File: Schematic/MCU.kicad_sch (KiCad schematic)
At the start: 21 parts, among them IC3 STM32H743VIT6, J1 USB_C_Receptacle_USB2.0_16P, SW1 TS24CA, Y1 8MHz

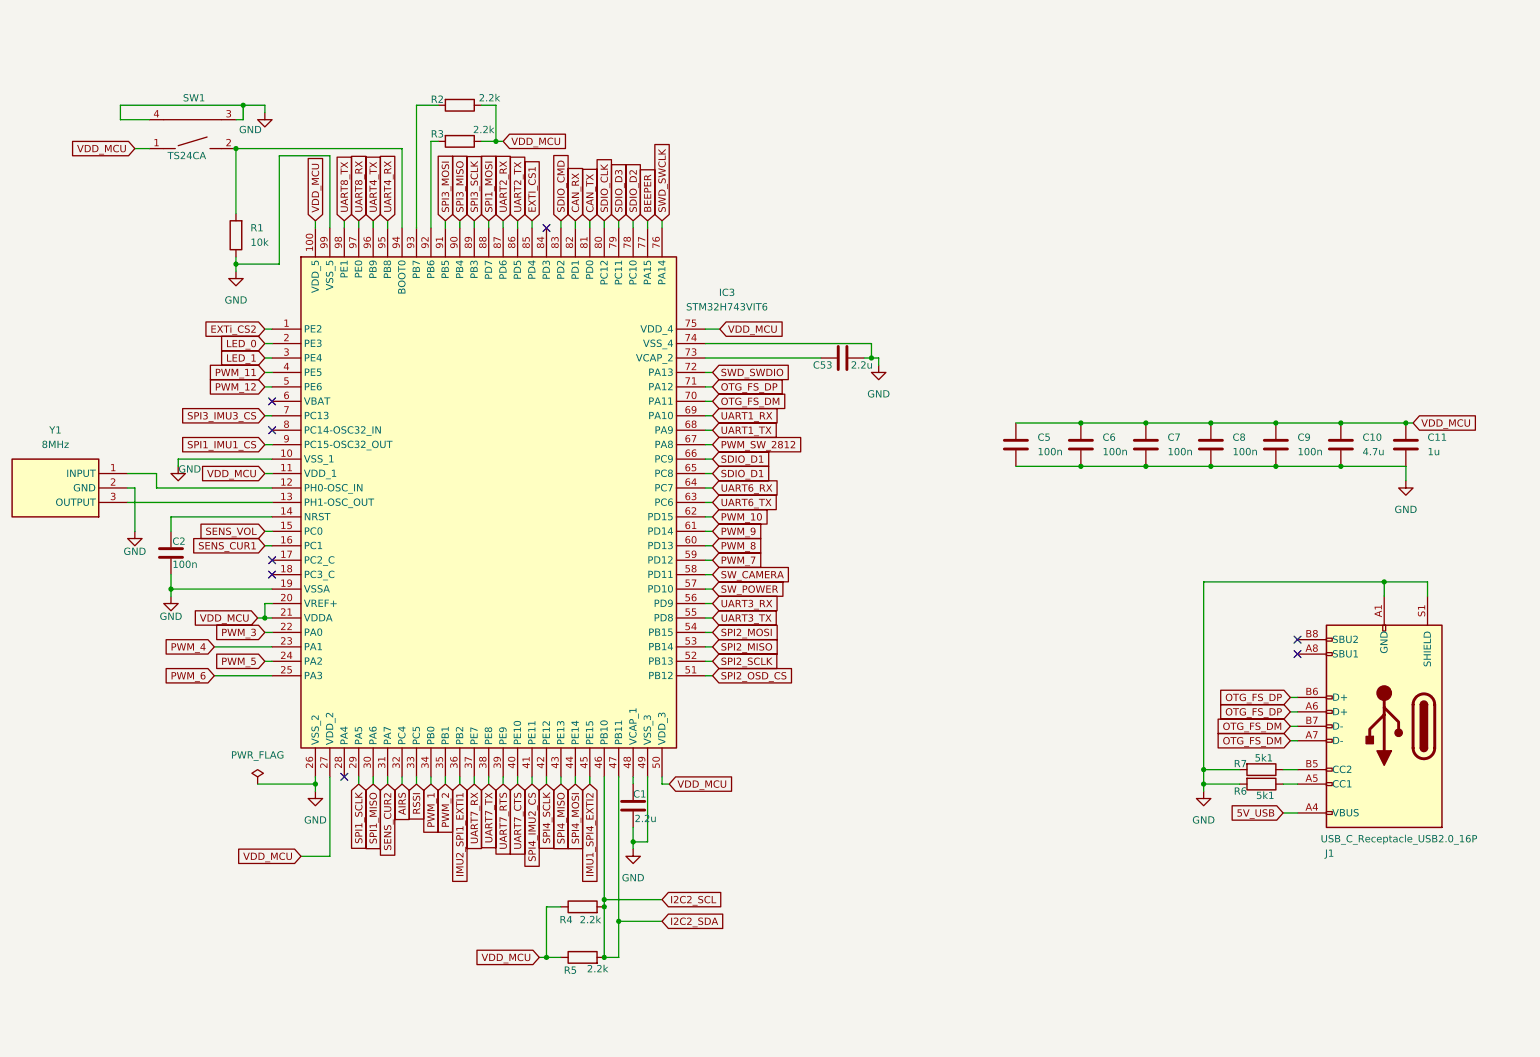
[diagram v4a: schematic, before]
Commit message: Refactor schematic files and update component placements
- Adjusted component positions in osd.kicad_sch for better layout.
- Added new junctions and wires in rf_rx.kicad_sch to improve connectivity.
- Introduced additional junctions and wires in sensors.kicad_sch for enhanced signal routing.
- Removed outdated backup file fch7-2025-11-18_191836.zip and added new backup fch7-2025-11-27_202230.zip.
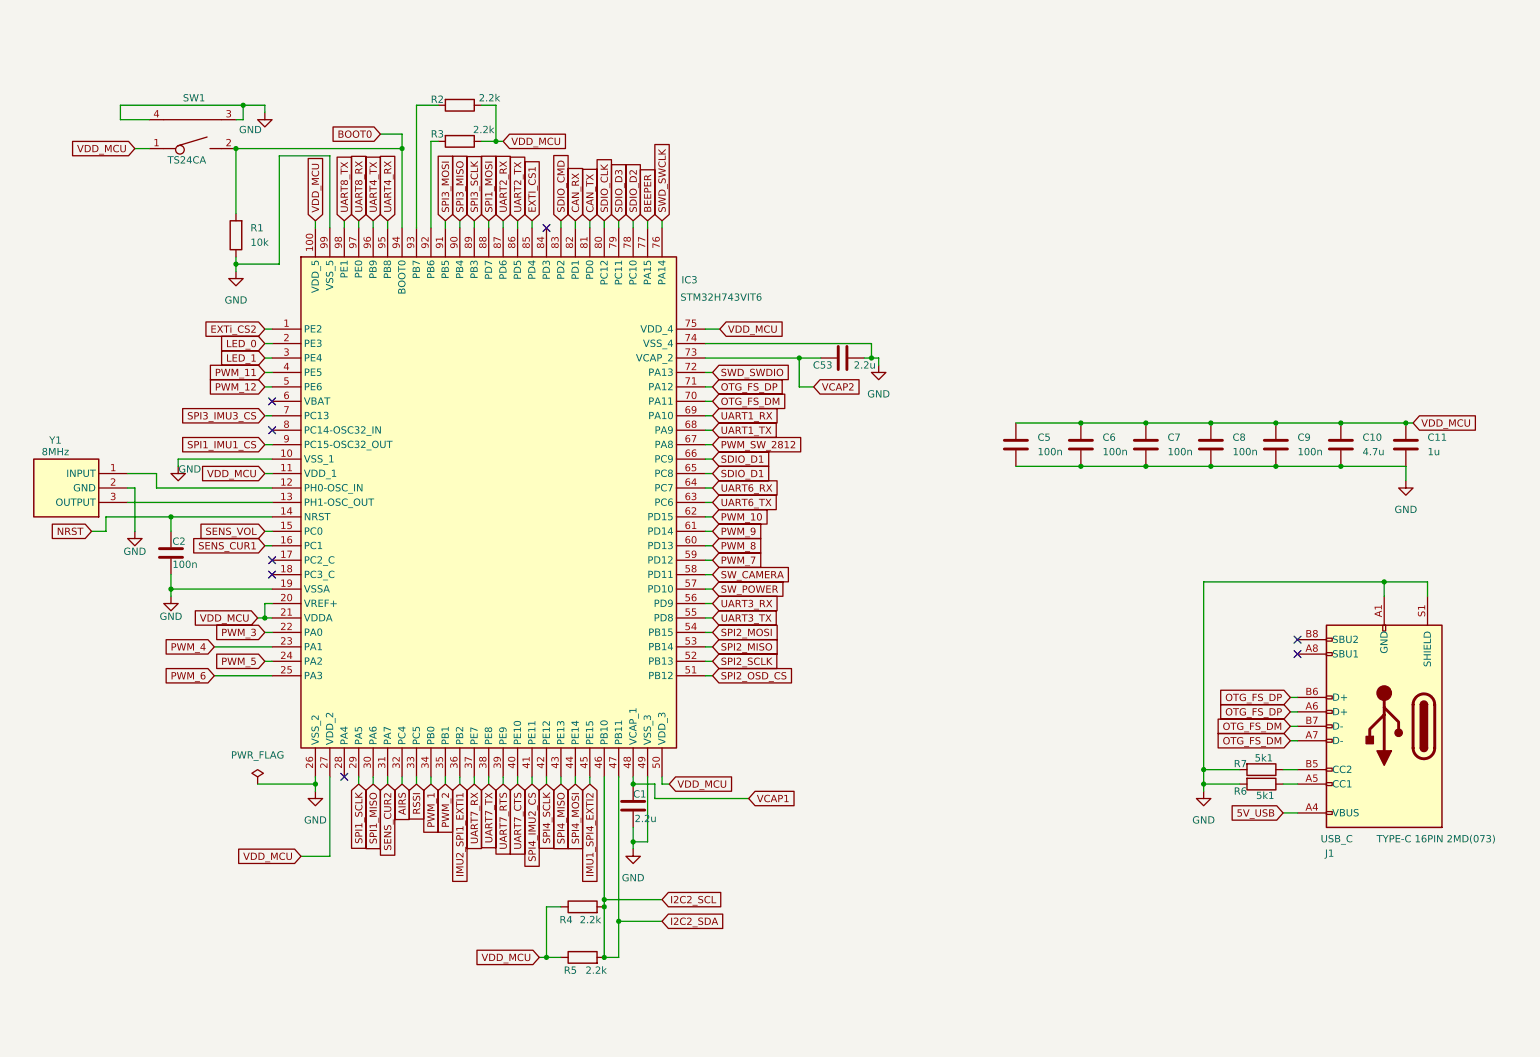
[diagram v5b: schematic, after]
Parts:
- J1: value USB_C_Receptacle_USB2.0_16P -> USB_C
- SW1: footprint fch7_fp:SW-SMD_2P-TS24CA -> ProLib_pcs_2025-11-24:SW-SMD_2P-TS24CA
- Y1: footprint fch7_fp:CSTNE8M00G55Z000R0 -> CSTNE8M00G55Z000R0
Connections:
- net NRST: now reaches C2.1, IC3.14 (NRST)
- net BOOT0: now reaches IC3.94 (BOOT0), R1.2, SW1.2
- net VCAP2: now reaches C53.1, IC3.73 (VCAP_2)
- net VCAP1: now reaches C1.1, IC3.48 (VCAP_1)
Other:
- moved on the sheet: Y1
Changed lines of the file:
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@@
 	)
 	(junction
+		(at 127 148.59)
+		(diameter 0)
+		(color 0 0 0 0)
+	)
+	(junction
 		(at 205.74 85.09)
 		(diameter 0)
@@
 	)
 	(junction
+		(at 156.21 73.66)
+		(diameter 0)
+		(color 0 0 0 0)
+	)
+	(junction
 		(at 259.08 113.03)
 		(diameter 0)
@@
 	)
 	(junction
+		(at 86.36 36.83)
+		(diameter 0)
+		(color 0 0 0 0)
+	)
+	(junction
 		(at 217.17 85.09)
 		(diameter 0)
@@
 	)
 	(junction
+		(at 45.72 101.6)
+		(diameter 0)
+		(color 0 0 0 0)
+	)
+	(junction
 		(at 111.76 179.07)
 		(diameter 0)
@@
 	(wire
 		(pts
+			(xy 156.21 78.74) (xy 156.21 73.66)
+		)
+		(stroke
+			(width 0)
+			(type default)
+		)
+	)
+	(wire
+		(pts
+			(xy 158.75 78.74) (xy 156.21 78.74)
+		)
+		(stroke
+			(width 0)
+			(type default)
+		)
+	)
+	(wire
+		(pts
 			(xy 60.96 119.38) (xy 62.23 119.38)
 		)
@@
 	(wire
 		(pts
+			(xy 147.32 151.13) (xy 130.81 151.13)
+		)
+		(stroke
+			(width 0)
+			(type default)
+		)
+	)
+	(wire
+		(pts
 			(xy 64.77 38.1) (xy 64.77 57.15)
 		)
@@
 	(wire
 		(pts
-			(xy 139.7 73.66) (xy 160.02 73.66)
+			(xy 139.7 73.66) (xy 156.21 73.66)
 		)
 		(stroke
@@
 	(wire
 		(pts
+			(xy 34.29 101.6) (xy 45.72 101.6)
+		)
+		(stroke
+			(width 0)
+			(type default)
+		)
+	)
+	(wire
+		(pts
 			(xy 101.6 49.53) (xy 101.6 50.8)
 		)
@@
 	(wire
 		(pts
+			(xy 130.81 148.59) (xy 127 148.59)
+		)
+		(stroke
+			(width 0)
+			(type default)
+		)
+	)
+	(wire
+		(pts
 			(xy 110.49 179.07) (xy 111.76 179.07)
 		)
@@
 	(wire
 		(pts
+			(xy 86.36 34.29) (xy 86.36 36.83)
+		)
+		(stroke
+			(width 0)
+			(type default)
+		)
+	)
+	(wire
+		(pts
 			(xy 73.66 38.1) (xy 64.77 38.1)
 		)
@@
 	(wire
 		(pts
+			(xy 130.81 151.13) (xy 130.81 148.59)
+		)
+		(stroke
+			(width 0)
+			(type default)
+		)
+	)
+	(wire
+		(pts
 			(xy 62.23 88.9) (xy 63.5 88.9)
 		)
@@
 	(wire
 		(pts
+			(xy 82.55 34.29) (xy 86.36 34.29)
+		)
+		(stroke
+			(width 0)
+			(type default)
+		)
+	)
+	(wire
+		(pts
 			(xy 127 158.75) (xy 129.54 158.75)
 		)
@@
 	(wire
 		(pts
+			(xy 156.21 73.66) (xy 160.02 73.66)
+		)
+		(stroke
+			(width 0)
+			(type default)
+		)
+	)
+	(wire
+		(pts
 			(xy 73.66 147.32) (xy 73.66 161.29)
 		)
@@
 	(wire
 		(pts
+			(xy 31.75 104.14) (xy 34.29 104.14)
+		)
+		(stroke
+			(width 0)
+			(type default)
+		)
+	)
+	(wire
+		(pts
 			(xy 104.14 49.53) (xy 104.14 50.8)
 		)
@@
 	(wire
 		(pts
+			(xy 34.29 104.14) (xy 34.29 101.6)
+		)
+		(stroke
+			(width 0)
+			(type default)
+		)
+	)
+	(wire
+		(pts
 			(xy 62.23 93.98) (xy 63.5 93.98)
 		)
@@
 		)
 	)
+	(global_label "NRST"
+		(shape input)
+		(at 31.75 104.14 180)
+		(fields_autoplaced yes)
+		(effects
+			(font
+				(size 1.27 1.27)
+			)
+			(justify right)
+		)
+		(property "Intersheetrefs" "${INTERSHEET_REFS}"
+			(at 23.9872 104.14 0)
+			(effects
+				(font
+					(size 1.27 1.27)
+				)
+				(justify right)
+				(hide yes)
+			)
+		)
+	)
 	(global_label "OTG_FS_DP"
 		(shape input)
@@
 		)
 	)
+	(global_label "VCAP2"
+		(shape input)
+		(at 158.75 78.74 0)
+		(fields_autoplaced yes)
+		(effects
+			(font
+				(size 1.27 1.27)
+			)
+			(justify left)
+		)
+		(property "Intersheetrefs" "${INTERSHEET_REFS}"
+			(at 167.6619 78.74 0)
+			(effects
+				(font
+					(size 1.27 1.27)
+				)
+				(justify left)
+				(hide yes)
+			)
+		)
+	)
 	(global_label "SPI2_SCLK"
 		(shape input)
@@
 		)
 	)
+	(global_label "VCAP1"
+		(shape input)
+		(at 147.32 151.13 0)
+		(fields_autoplaced yes)
+		(effects
+			(font
+				(size 1.27 1.27)
+			)
+			(justify left)
+		)
+		(property "Intersheetrefs" "${INTERSHEET_REFS}"
+			(at 156.2319 151.13 0)
+			(effects
+				(font
+					(size 1.27 1.27)
+				)
+				(justify left)
+				(hide yes)
+			)
+		)
+	)
 	(global_label "SPI1_MOSI"
 		(shape input)
@@
 		)
 	)
+	(global_label "BOOT0"
+		(shape input)
+		(at 82.55 34.29 180)
+		(fields_autoplaced yes)
+		(effects
+			(font
+				(size 1.27 1.27)
+			)
+			(justify right)
+		)
+		(property "Intersheetrefs" "${INTERSHEET_REFS}"
+			(at 73.4567 34.29 0)
+			(effects
+				(font
+					(size 1.27 1.27)
+				)
+				(justify right)
+				(hide yes)
+			)
+		)
+	)
 	(global_label "SPI3_MOSI"
 		(shape input)
@@
 			)
 		)
-		(property "Value" "USB_C_Receptacle_USB2.0_16P"
+		(property "Value" "USB_C"
 			(at 247.904 158.242 0)
 			(effects
@@
 		)
 		(property "MPN" "TYPE-C 16PIN 2MD(073)"
-			(at 259.08 138.43 0)
+			(at 268.224 158.242 0)
 			(effects
 				(font
 					(size 1.27 1.27)
 				)
-				(hide yes)
 			)
 		)
@@
 		(on_board yes)
 		(dnp no)
-		(fields_autoplaced yes)
 		(property "Reference" "Y1"
-			(at 25.4 86.36 0)
+			(at 25.4 88.138 0)
 			(effects
 				(font
@@
 		)
 		(property "Value" "8MHz"
-			(at 25.4 88.9 0)
+			(at 25.4 90.17 0)
 			(effects
 				(font
@@
 			)
 		)
-		(property "Footprint" "fch7_fp:CSTNE8M00G55Z000R0"
+		(property "Footprint" "CSTNE8M00G55Z000R0"
 			(at 16.51 4.14 0)
 			(effects
@@
 		)
 		(property "Value" "2.2u"
-			(at 169.164 74.93 90)
+			(at 169.672 74.93 90)
 			(effects
 				(font
@@
 		)
 		(property "Value" "2.2k"
-			(at 118.872 181.102 90)
+			(at 118.618 181.356 90)
 			(effects
 				(font
@@
 		)
 		(property "Value" "TS24CA"
-			(at 48.514 38.1 0)
+			(at 48.514 38.862 0)
 			(effects
 				(font
@@
 			)
 		)
-		(property "Footprint" "fch7_fp:SW-SMD_2P-TS24CA"
+		(property "Footprint" "ProLib_pcs_2025-11-24:SW-SMD_2P-TS24CA"
 			(at 48.768 27.686 0)
 			(effects
@@
 		(on_board yes)
 		(dnp no)
-		(fields_autoplaced yes)
 		(property "Reference" "IC3"
-			(at 143.51 62.1598 0)
+			(at 136.906 59.944 0)
 			(effects
 				(font
@@
 		)
 		(property "Value" "STM32H743VIT6"
-			(at 143.51 64.6998 0)
+			(at 142.494 62.992 0)
 			(effects
 				(font

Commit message: Refactor code structure for improved readability and maintainability
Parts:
- SW1: footprint ProLib_pcs_2025-11-24:SW-SMD_2P-TS24CA -> fch7_fp:SW-SMD_2P-TS24CA
- Y1: footprint CSTNE8M00G55Z000R0 -> fch7_fp:CSTNE8M00G55Z000R0
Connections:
- net I2C2_SCL: no longer IC3.47 (PB11), R5.2
- new net I2C2_SDA: IC3.47 (PB11), R5.2
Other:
- note added: "Decoupling capacitors for MCU pins"
- moved on the sheet: C10, C11, C5, C6, C7, C8, C9, R4

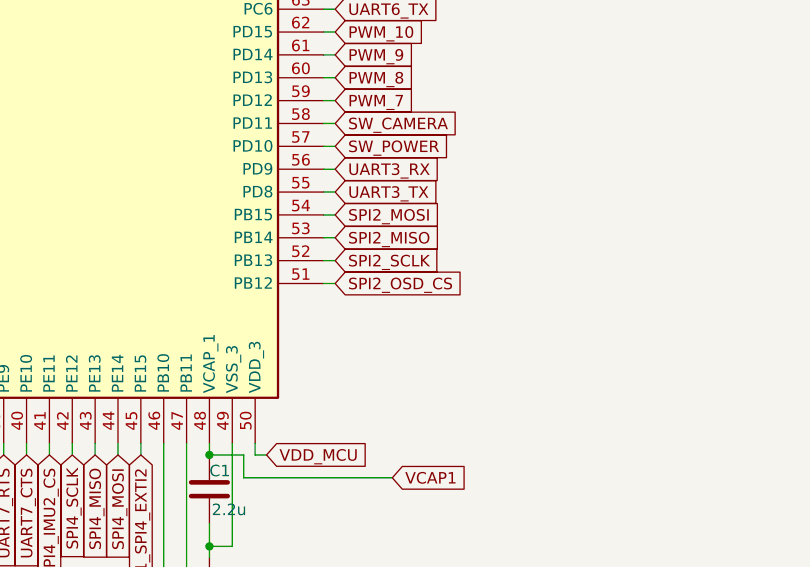
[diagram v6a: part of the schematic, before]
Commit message: Removed useless analog OSD and VTX conneections to support only digital DJI
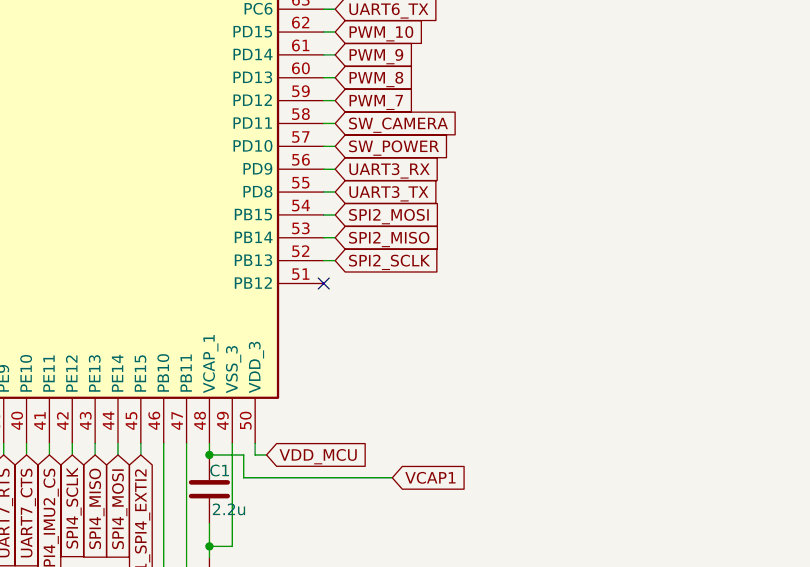
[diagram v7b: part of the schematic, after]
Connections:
- net SPI2_OSD_CS: no longer names the net of IC3.51 (PB12)
- no-connect marks 8 -> 9
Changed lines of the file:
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@@
 	)
 	(no_connect
+		(at 139.7 129.54)
+	)
+	(no_connect
 		(at 111.76 50.8)
 	)
@@
 	(wire
 		(pts
-			(xy 139.7 129.54) (xy 140.97 129.54)
-		)
-		(stroke
-			(width 0)
-			(type default)
-		)
-	)
-	(wire
-		(pts
 			(xy 227.33 146.05) (xy 227.33 148.59)
 		)
@@
 			(effects
 				(font
-					(size 1.27 1.27)
-				)
-				(justify left)
-				(hide yes)
-			)
-		)
-	)
-	(global_label "SPI2_OSD_CS"
-		(shape input)
-		(at 140.97 129.54 0)
-		(fields_autoplaced yes)
-		(effects
-			(font
-				(size 1.27 1.27)
-			)
-			(justify left)
-		)
-		(property "Intersheetrefs" "${INTERSHEET_REFS}"
-			(at 156.4737 129.54 0)
-			(effects
-				(font

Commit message: Refactor code structure for improved readability and maintainability
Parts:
- removed IC3: STM32H743VIT6, fch7_fp:LQFP-100_14x14mm_P0.5mm_STM32H743, symbol STM32H743VIT6:STM32H743VIT6
- removed J1: USB_C, fch7_fp:USB-C-SMD_TYPE-C-6PIN-2MD-073, symbol Connector:USB_C_Receptacle_USB2.0_16P
- removed SW1: TS24CA, fch7_fp:SW-SMD_2P-TS24CA, symbol fch7_sym:TS24CA
- removed Y1: 8MHz, fch7_fp:CSTNE8M00G55Z000R0, symbol CSTNE8M00G55Z000R0:CSTNE8M00G55Z000R0
- added IC3: STM32H743VIT6, fch7_fp:LQFP-100_14x14mm_P0.5mm_STM32H743, symbol fclib:STM32H743VIT6
- added SW1: TS24CA, fch7_fp:SW-SMD_2P-TS24CA, symbol fclib:TS24CA
- added USB1: USB-C-SMD_TYPE-C-6PIN-2MD-073, fch7_fp:USB-C-SMD_TYPE-C-6PIN-2MD-073, symbol fclib:TYPE-C 16PIN 2MD(073)
- added Y1: 8MHz, fch7_fp:CSTNE8M00G55Z000R0, symbol fclib:CSTNE8M00G55Z000R0
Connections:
- net 5V_USB: now also USB1.11 (VBUS), USB1.2 (VBUS)
- net AIRS: now also IC3.32 (PC4)
- net BEEPER: now also IC3.77 (PA15)
- net BOOT0: now also IC3.94 (BOOT0), SW1.2
- net CAN_RX: now also IC3.82 (PD1)
- net CAN_TX: now also IC3.81 (PD0)
- net EXTI_CS1: now also IC3.85 (PD4)
- net EXTi_CS2: now also IC3.1 (PE2)
- net GND: now also IC3.10 (VSS_1), IC3.19 (VSSA), IC3.26 (VSS_2), IC3.49 (VSS_3), IC3.74 (VSS_4), IC3.99 (VSS_5), SW1.3, SW1.4, USB1.1 (GND), USB1.12 (GND), USB1.13 (SHELL), USB1.14 (SHELL), Y1.2 (GND)
- net I2C2_SCL: now also IC3.46 (PB10)
- net I2C2_SDA: now also IC3.47 (PB11)
- net IMU1_SPI4_EXTI2: now also IC3.45 (PE15)
- net IMU2_SPI1_EXTI1: now also IC3.36 (PB2)
- net LED_0: now also IC3.2 (PE3)
- net LED_1: now also IC3.3 (PE4)
- net NRST: now also IC3.14 (NRST)
- net OTG_FS_DM: now also IC3.70 (PA11), USB1.5 (DN2), USB1.7 (DN1)
- net OTG_FS_DP: now also IC3.71 (PA12), USB1.6 (DP1), USB1.8 (DP2)
- net PWM_1: now also IC3.34 (PB0)
- net PWM_10: now also IC3.62 (PD15)
- net PWM_11: now also IC3.4 (PE5)
- net PWM_12: now also IC3.5 (PE6)
- net PWM_2: now also IC3.35 (PB1)
- net PWM_3: now also IC3.22 (PA0)
- net PWM_4: now also IC3.23 (PA1)
- net PWM_5: now also IC3.24 (PA2)
- net PWM_6: now also IC3.25 (PA3)
- net PWM_7: now also IC3.59 (PD12)
- net PWM_8: now also IC3.60 (PD13)
- net PWM_9: now also IC3.61 (PD14)
- net PWM_SW_2812: now also IC3.67 (PA8)
- net RSSI: now also IC3.33 (PC5)
- net SDIO_CLK: now also IC3.80 (PC12)
- net SDIO_CMD: now also IC3.83 (PD2)
- net SDIO_D1: now also IC3.65 (PC8), IC3.66 (PC9)
- net SDIO_D2: now also IC3.78 (PC10)
- net SDIO_D3: now also IC3.79 (PC11)
- net SENS_CUR1: now also IC3.16 (PC1)
- net SENS_CUR2: now also IC3.31 (PA7)
- net SENS_VOL: now also IC3.15 (PC0)
- net SPI1_IMU1_CS: now also IC3.9 (PC15-OSC32_OUT)
- net SPI1_MISO: now also IC3.30 (PA6)
- net SPI1_MOSI: now also IC3.88 (PD7)
- net SPI1_SCLK: now also IC3.29 (PA5)
- net SPI2_MISO: now also IC3.53 (PB14)
- net SPI2_MOSI: now also IC3.54 (PB15)
- net SPI2_SCLK: now also IC3.52 (PB13)
- net SPI3_IMU3_CS: now also IC3.7 (PC13)
- net SPI3_MISO: now also IC3.90 (PB4)
- net SPI3_MOSI: now also IC3.91 (PB5)
- net SPI3_SCLK: now also IC3.89 (PB3)
- net SPI4_IMU2_CS: now also IC3.41 (PE11)
- net SPI4_MISO: now also IC3.43 (PE13)
- net SPI4_MOSI: now also IC3.44 (PE14)
- net SPI4_SCLK: now also IC3.42 (PE12)
- net SWD_SWCLK: now also IC3.76 (PA14)
- net SWD_SWDIO: now also IC3.72 (PA13)
- net SW_CAMERA: now also IC3.58 (PD11)
- net SW_POWER: now also IC3.57 (PD10)
- net UART1_RX: now also IC3.69 (PA10)
- net UART1_TX: now also IC3.68 (PA9)
- net UART2_RX: now also IC3.87 (PD6)
- net UART2_TX: now also IC3.86 (PD5)
- net UART3_RX: now also IC3.56 (PD9)
- net UART3_TX: now also IC3.55 (PD8)
- net UART4_RX: now also IC3.95 (PB8)
- net UART4_TX: now also IC3.96 (PB9)
- net UART6_RX: now also IC3.64 (PC7)
- net UART6_TX: now also IC3.63 (PC6)
- net UART7_CTS: now also IC3.40 (PE10)
- net UART7_RTS: now also IC3.39 (PE9)
- net UART7_RX: now also IC3.37 (PE7)
- net UART7_TX: now also IC3.38 (PE8)
- net UART8_RX: now also IC3.97 (PE0)
- net UART8_TX: now also IC3.98 (PE1)
- net VCAP1: now also IC3.48 (VCAP_1)
- net VCAP2: now also IC3.73 (VCAP_2)
- net VDD_MCU: now also IC3.100 (VDD_5), IC3.11 (VDD_1), IC3.20 (VREF+), IC3.21 (VDDA), IC3.27 (VDD_2), IC3.50 (VDD_3), IC3.75 (VDD_4), SW1.1
- net at R6.1: now also USB1.10 (CC2)
- net at R7.1: now also USB1.4 (CC1)
- net at R2.2: now also IC3.93 (PB7)
- net at R3.2: now also IC3.92 (PB6)
- new net: IC3.12 (PH0-OSC_IN), Y1.1 (INPUT)
- new net: IC3.13 (PH1-OSC_OUT), Y1.3 (OUTPUT)
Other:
- moved on the sheet: R7
